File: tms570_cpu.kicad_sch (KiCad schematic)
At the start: 34 parts, among them J2 CONN_02X05, U2 TMS570LS0914PGE

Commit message: Finish up and clean up a lot of things
Signed-off-by: Corey Minyard <corey@minyard.net>
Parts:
- added R131: 33, Resistor_SMD:R_0603_1608Metric_Pad0.98x0.95mm_HandSolder, symbol Device:R
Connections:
- net AX5043_CLK: now also R131.1; no longer U2.95 (MIBSPI1CLK)
- net AX5043_EN_RX4: now reaches U2.32 (MIBSPI5NCS_0)
- net AX5043_EN_RX3: now reaches U2.33 (N2HET1_7)
- net AX5043_EN_RX2: now reaches U2.35 (N2HET1_9)
- net AX5043_EN_RX1: now reaches U2.36 (N2HET1_4)
- new net: R131.2, U2.95 (MIBSPI1CLK)
- no-connect marks 36 -> 32
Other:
- note added: "See document on AX5043 clock signal handling."
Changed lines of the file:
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@@
 		)
 	)
+	(text "See document on \nAX5043 clock\nsignal handling."
+		(exclude_from_sim no)
+		(at 210.566 25.654 90)
+		(effects
+			(font
+				(size 1.524 1.524)
+			)
+		)
+	)
 	(text "TCK"
 		(exclude_from_sim no)
@@
 	)
 	(no_connect
-		(at 260.35 204.47)
-	)
-	(no_connect
 		(at 260.35 72.39)
 	)
@@
 	)
 	(no_connect
-		(at 252.73 204.47)
-	)
-	(no_connect
 		(at 219.71 204.47)
 	)
@@
 	)
 	(no_connect
-		(at 257.81 204.47)
-	)
-	(no_connect
-		(at 250.19 204.47)
-	)
-	(no_connect
 		(at 255.27 72.39)
 	)
@@
 	(wire
 		(pts
-			(xy 204.47 72.39) (xy 204.47 59.69)
+			(xy 204.47 72.39) (xy 204.47 38.1)
 		)
 		(stroke
@@
 	(wire
 		(pts
+			(xy 257.81 204.47) (xy 257.81 215.9)
+		)
+		(stroke
+			(width 0)
+			(type default)
+		)
+	)
+	(wire
+		(pts
 			(xy 227.33 204.47) (xy 227.33 251.46)
 		)
@@
 	(wire
 		(pts
+			(xy 250.19 204.47) (xy 250.19 215.9)
+		)
+		(stroke
+			(width 0)
+			(type default)
+		)
+	)
+	(wire
+		(pts
 			(xy 152.4 218.44) (xy 212.09 218.44)
 		)
@@
 	(wire
 		(pts
+			(xy 260.35 204.47) (xy 260.35 215.9)
+		)
+		(stroke
+			(width 0)
+			(type default)
+		)
+	)
+	(wire
+		(pts
 			(xy 217.17 59.69) (xy 217.17 72.39)
 		)
@@
 	(wire
 		(pts
+			(xy 204.47 30.48) (xy 204.47 29.21)
+		)
+		(stroke
+			(width 0)
+			(type default)
+		)
+	)
+	(wire
+		(pts
 			(xy 237.49 207.01) (xy 237.49 209.55)
 		)
@@
 	(wire
 		(pts
+			(xy 252.73 204.47) (xy 252.73 215.9)
+		)
+		(stroke
+			(width 0)
+			(type default)
+		)
+	)
+	(wire
+		(pts
 			(xy 245.11 204.47) (xy 245.11 259.08)
 		)
@@
 		)
 	)
+	(global_label "AX5043_EN_RX1"
+		(shape input)
+		(at 260.35 215.9 270)
+		(fields_autoplaced yes)
+		(effects
+			(font
+				(size 1.524 1.524)
+			)
+			(justify right)
+		)
+		(property "Intersheetrefs" "${INTERSHEET_REFS}"
+			(at 260.35 236.9846 90)
+			(effects
+				(font
+					(size 1.27 1.27)
+				)
+				(justify right)
+				(hide yes)
+			)
+		)
+	)
 	(global_label "VER_BIT2"
 		(shape input)
@@
 		)
 	)
+	(global_label "AX5043_EN_RX3"
+		(shape input)
+		(at 252.73 215.9 270)
+		(fields_autoplaced yes)
+		(effects
+			(font
+				(size 1.524 1.524)
+			)
+			(justify right)
+		)
+		(property "Intersheetrefs" "${INTERSHEET_REFS}"
+			(at 252.73 236.9846 90)
+			(effects
+				(font
+					(size 1.27 1.27)
+				)
+				(justify right)
+				(hide yes)
+			)
+		)
+	)
 	(global_label "MRAM_MISO"
 		(shape input)
@@
 		)
 	)
+	(global_label "AX5043_EN_RX2"
+		(shape input)
+		(at 257.81 215.9 270)
+		(fields_autoplaced yes)
+		(effects
+			(font
+				(size 1.524 1.524)
+			)
+			(justify right)
+		)
+		(property "Intersheetrefs" "${INTERSHEET_REFS}"
+			(at 257.81 236.9846 90)
+			(effects
+				(font
+					(size 1.27 1.27)
+				)
+				(justify right)
+				(hide yes)
+			)
+		)
+	)
 	(global_label "VER_BIT0"
 		(shape input)
@@
 	(global_label "AX5043_CLK"
 		(shape input)
-		(at 204.47 59.69 90)
+		(at 204.47 29.21 90)
 		(fields_autoplaced yes)
 		(effects
@@
 		)
 		(property "Intersheetrefs" "${INTERSHEET_REFS}"
-			(at 204.47 42.8871 90)
+			(at 204.47 12.4071 90)
 			(effects
 				(font
@@
 		)
 	)
+	(global_label "AX5043_EN_RX4"
+		(shape input)
+		(at 250.19 215.9 270)
+		(fields_autoplaced yes)
+		(effects
+			(font
+				(size 1.524 1.524)
+			)
+			(justify right)
+		)
+		(property "Intersheetrefs" "${INTERSHEET_REFS}"
+			(at 250.19 236.9846 90)
+			(effects
+				(font
+					(size 1.27 1.27)
+				)
+				(justify right)
+				(hide yes)
+			)
+		)
+	)
 	(symbol
 		(lib_id "PACSAT_ICs:TMS570LS0914PGE")
@@
 					(unit 1)
 				)
+			)
+		)
+	)
+	(symbol
+		(lib_id "Device:R")
+		(at 204.47 34.29 0)
+		(unit 1)
+		(exclude_from_sim no)
+		(in_bom yes)
+		(on_board yes)
+		(dnp no)
+		(property "Reference" "R131"
+			(at 196.85 33.02 0)
+			(effects
+				(font
+					(size 1.27 1.27)
+				)
+				(justify left)
+			)
+		)
+		(property "Value" "33"
+			(at 198.755 34.925 0)
+			(effects
+				(font
+					(size 1.27 1.27)
+				)
+				(justify left)
+			)
+		)
+		(property "Footprint" "Resistor_SMD:R_0603_1608Metric_Pad0.98x0.95mm_HandSolder"
+			(at 202.692 34.29 90)
+			(effects
+				(font
+					(size 1.27 1.27)
+				)
+				(hide yes)
+			)
+		)
+		(property "Datasheet" "~"
+			(at 204.47 34.29 0)
+			(effects
+				(font
+					(size 1.27 1.27)
+				)
+			)
+		)
+		(property "Description" ""
+			(at 204.47 34.29 0)
+			(effects
+				(font
+					(size 1.27 1.27)
+				)
+			)
+		)
+		(pin "1"
+		)
+		(pin "2"
+		)
+		(instances
+			(project "PacSat_AFSK"
+				(path "/cc9f42d2-6985-41ac-acab-5ab7b01c5b38/adf61ae3-df77-4e04-8bda-b4049a36fcf4"
+					(reference "R131")
+					(unit 1)
+				)

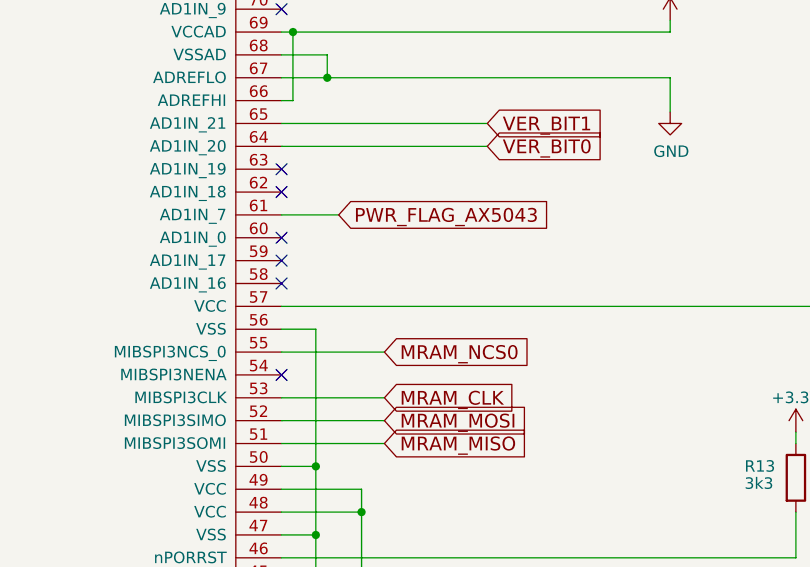
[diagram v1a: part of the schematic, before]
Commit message: Add a CPU thermsistor
Signed-off-by: Corey Minyard <corey@minyard.net>
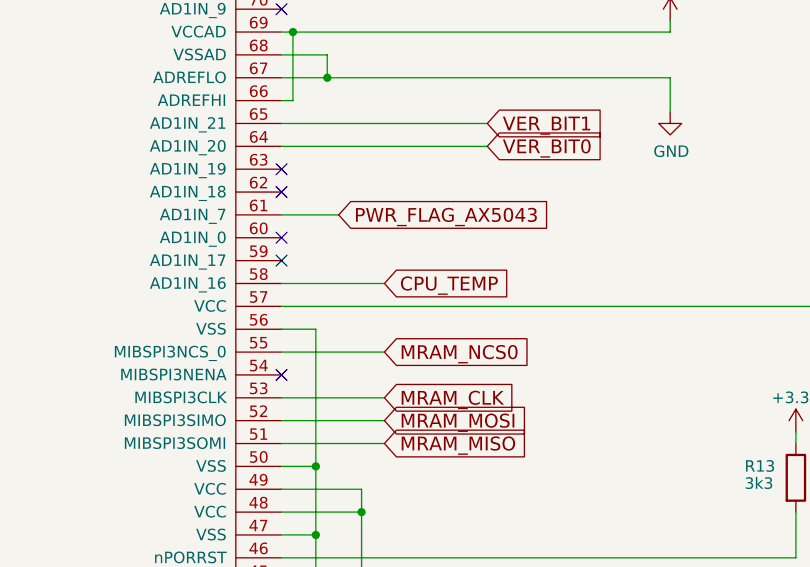
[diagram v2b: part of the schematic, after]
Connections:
- net CPU_TEMP: now reaches U2.58 (AD1IN_16)
- no-connect marks 32 -> 31
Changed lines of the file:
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@@
 	)
 	(no_connect
-		(at 281.94 129.54)
-	)
-	(no_connect
 		(at 281.94 182.88)
 	)
@@
 	(wire
 		(pts
+			(xy 281.94 129.54) (xy 293.37 129.54)
+		)
+		(stroke
+			(width 0)
+			(type default)
+		)
+	)
+	(wire
+		(pts
 			(xy 317.5 57.15) (xy 317.5 59.69)
 		)
@@
 				(hide yes)
 			)
+		)
+	)
+	(global_label "CPU_TEMP"
+		(shape input)
+		(at 293.37 129.54 0)
+		(fields_autoplaced yes)
+		(effects
+			(font
+				(size 1.524 1.524)
+			)
+			(justify left)
+		)
+		(property "Intersheetrefs" "${INTERSHEET_REFS}"
+			(at 307.7782 129.54 0)
+			(effects
+				(font
+					(size 1.27 1.27)
+				)
+				(justify left)
+				(hide yes)
+			)

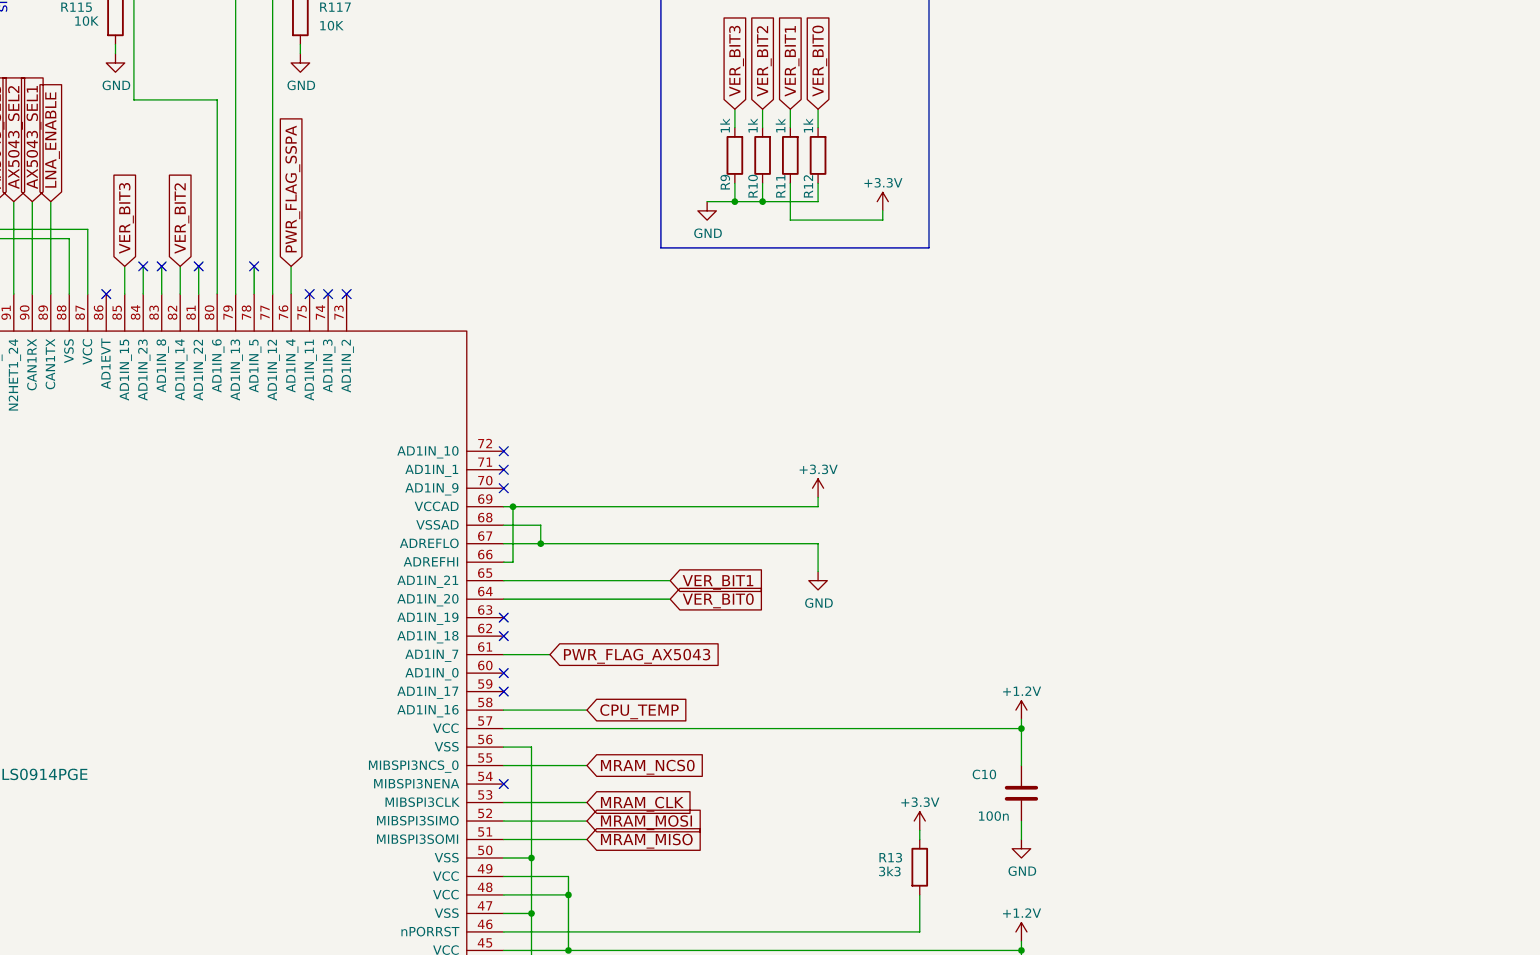
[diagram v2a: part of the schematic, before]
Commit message: Finished up the TX PA section.
Signed-off-by: Corey Minyard <corey@minyard.net>
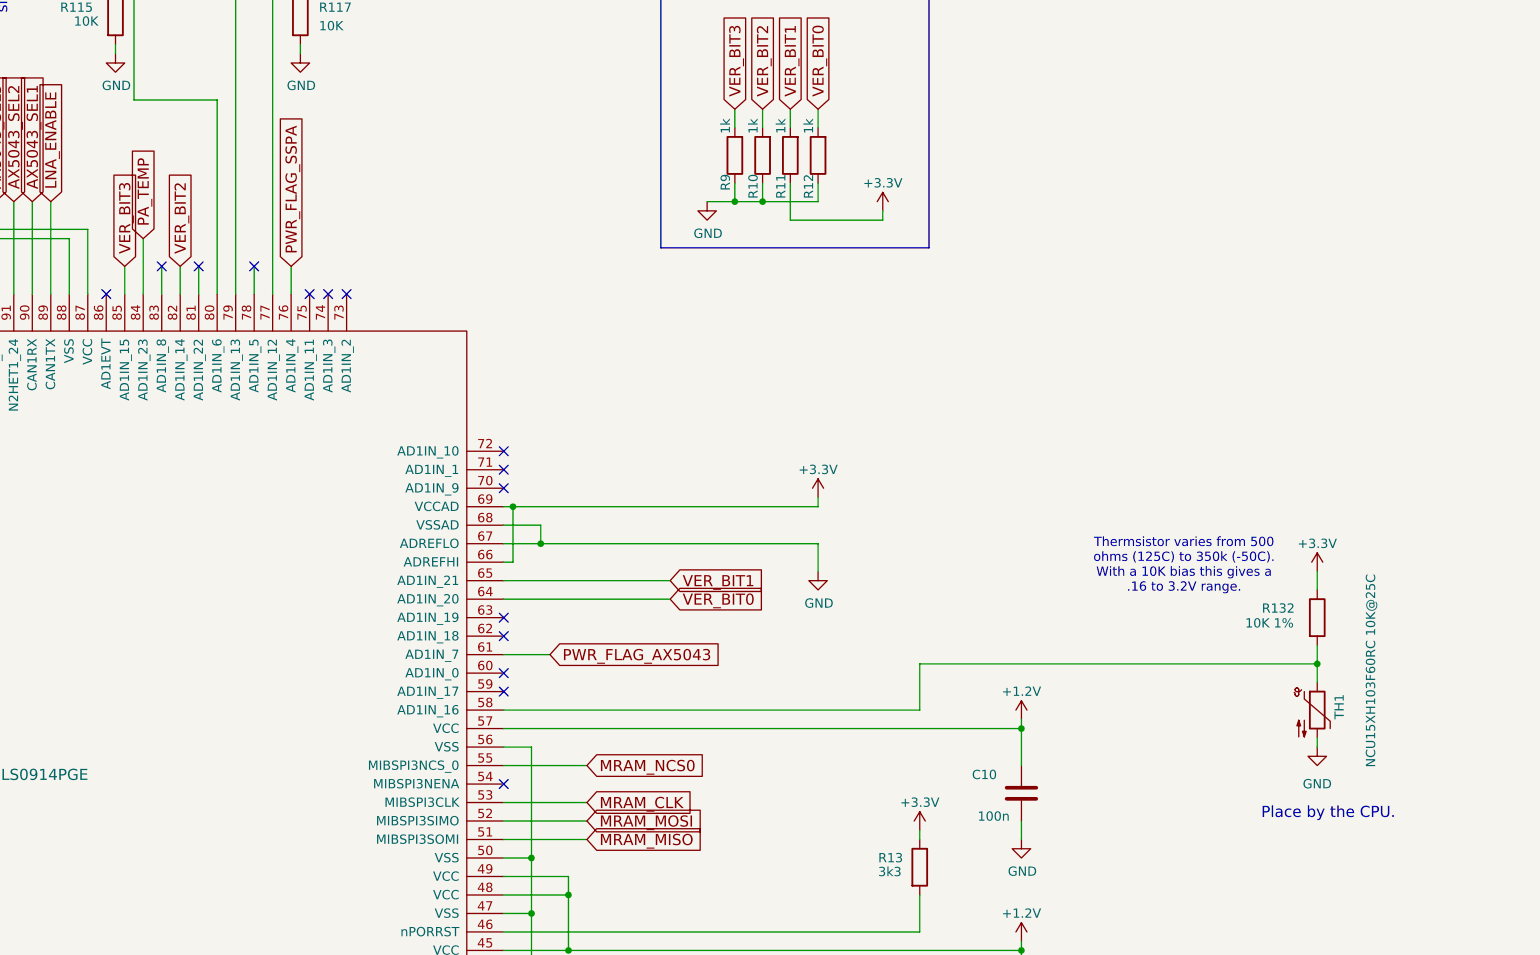
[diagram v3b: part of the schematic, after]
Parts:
- added R132: 10K 1%, Resistor_SMD:R_0603_1608Metric_Pad0.98x0.95mm_HandSolder, symbol Device:R
- added TH1: NCU15XH103F60RC 10K@25C, Resistor_SMD:R_0402_1005Metric, symbol Device:Thermistor_NTC
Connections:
- net +3.3V: now also R132.1
- net GND: now also TH1.2
- net PA_TEMP: now reaches U2.84 (AD1IN_23)
- net CPU_TEMP: no longer names the net of U2.58 (AD1IN_16)
- net CPU_TEMP: now also R132.2, TH1.1
- no-connect marks 31 -> 30
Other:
- note added: "Place by the CPU."
- note added: "Thermsistor varies from 500 ohms (125C) to 350k (-50C). With a 10K bias this gives a .16 to 3.2V range."

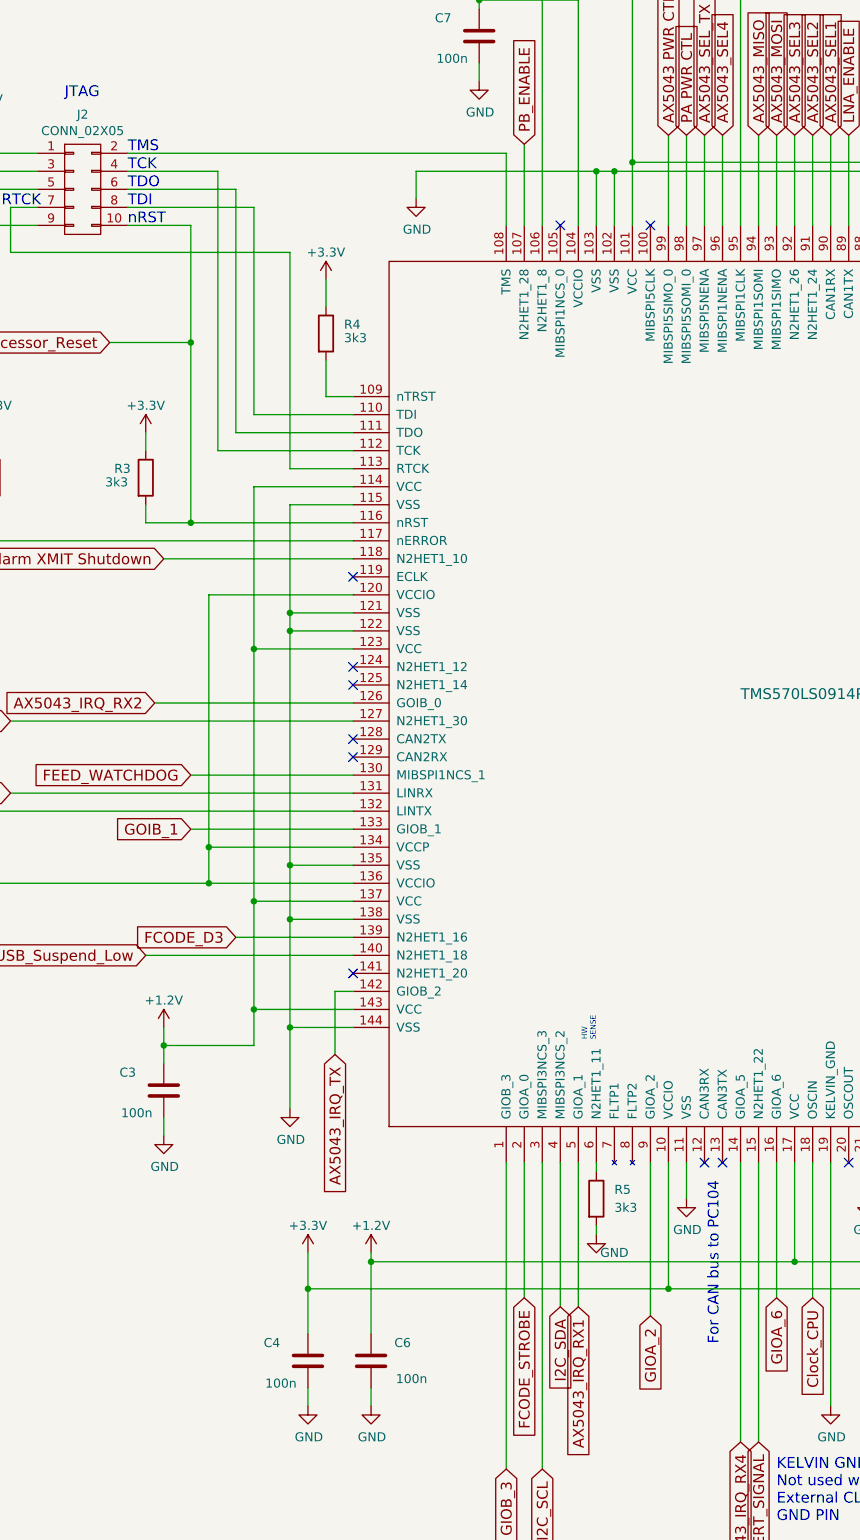
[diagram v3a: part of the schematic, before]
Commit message: Add resistors to the JTAG interface
They are supposed to be there.

Signed-off-by: Corey Minyard <corey@minyard.net>
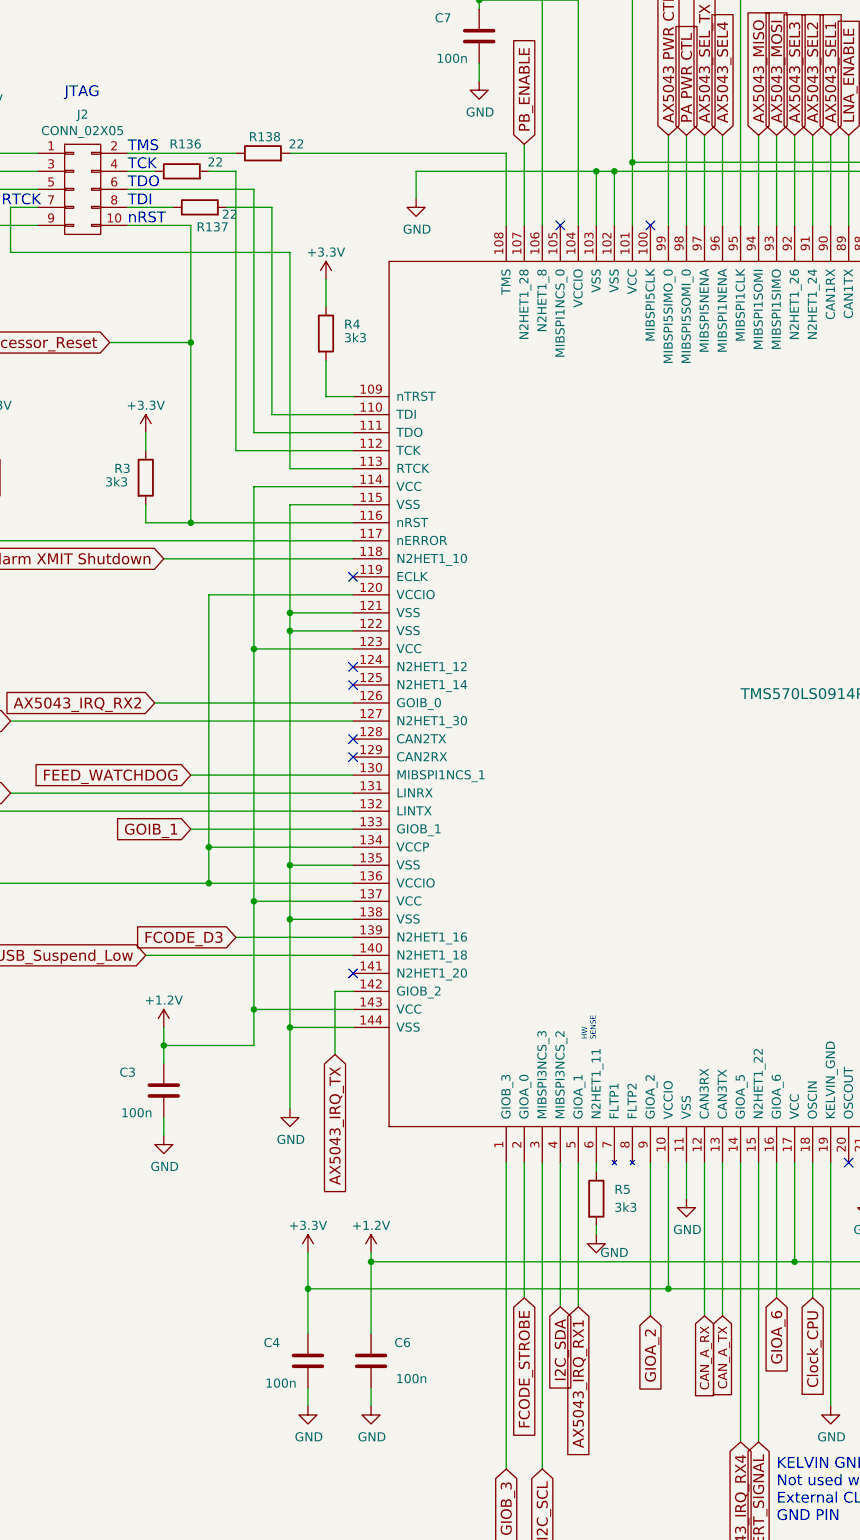
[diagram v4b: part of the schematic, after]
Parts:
- added R136, R137, R138: 22, Resistor_SMD:R_0603_1608Metric_Pad0.98x0.95mm_HandSolder, symbol Device:R
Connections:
- net at U2.108 (TMS): now also R138.2; no longer J2.2 (P2)
- net at U2.110 (TDI): now also R137.2; no longer J2.8 (P8)
- net at U2.112 (TCK): now also R136.2; no longer J2.4 (P4)
- net CAN_A_RX: now reaches U2.12 (CAN3RX)
- net CAN_A_TX: now reaches U2.13 (CAN3TX)
- new net: J2.2 (P2), R138.1
- new net: J2.4 (P4), R136.1
- new net: J2.8 (P8), R137.1
- no-connect marks 30 -> 28
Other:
- note removed: "For CAN bus to PC104"
